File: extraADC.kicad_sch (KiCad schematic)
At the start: 21 parts, among them J10 G125-MH11005L1P, Q14 DMP2160UWQ-7, U42 ADS1015BQDGSRQ1, U43 ADS1015BQDGSRQ1

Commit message: Add some notes on progress
Signed-off-by: Corey Minyard <corey@minyard.net>
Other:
- note added: "I2C addr = 0x48"
- note added: "I2C addr = 0x49"
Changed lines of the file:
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@@
 	(generator_version "9.0")
 	(paper "A4")
+	(text "I2C addr = 0x48"
+		(exclude_from_sim no)
+		(at 183.388 76.708 0)
+		(effects
+			(font
+				(size 1.524 1.524)
+			)
+		)
+	)
+	(text "I2C addr = 0x49"
+		(exclude_from_sim no)
+		(at 174.498 115.57 0)
+		(effects
+			(font
+				(size 1.524 1.524)
+			)
+		)
+	)
 	(junction
 		(at 160.02 66.04)

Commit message: Add licensing
Use CERN-OHL-W version 2

Signed-off-by: Corey Minyard <corey@minyard.net>
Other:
- company: (none) -> AMSAT-NA
- title: (none) -> Extra ADC handled by the Antenna Control Processor
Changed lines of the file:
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@@
 	(generator_version "10.0")
 	(paper "A4")
+	(title_block
+		(title "Extra ADC handled by the Antenna Control Processor")
+		(date "2026-08-20")
+		(rev "4.0")
+		(company "AMSAT-NA")
+		(comment 1 "AE5KM")
+		(comment 2 "Copyright Corey Minyard, 2026")
+		(comment 3 "Licensed under CERN-OHL-W version 2")
+	)
 	(text "I2C addr = 0x48"
 		(exclude_from_sim no)

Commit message: Rework the antenna controller power
Change the MOSFET + ferrite to an inrush-controlled chip on the antenna
controller power and remove the separate ADC power enable.  Just power
the ADCs with the antenna controller power, there wasn't much benefit in
separate power control for it.

Signed-off-by: Corey Minyard <corey@minyard.net>
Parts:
- removed FB10: 1KΩ@100MHz, Inductor_SMD:L_0603_1608Metric_Pad1.05x0.95mm_HandSolder, symbol Device:FerriteBead_Small
- removed Q14: DMP2160UWQ-7, Package_TO_SOT_SMD:SOT-323_SC-70, symbol Transistor_FET:Q_PMOS_GSD
- removed R176: 10KΩ, Resistor_SMD:R_0402_1005Metric_Pad0.72x0.64mm_HandSolder, symbol Device:R
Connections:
- net ADC_3.3V renamed ANT_3.3V

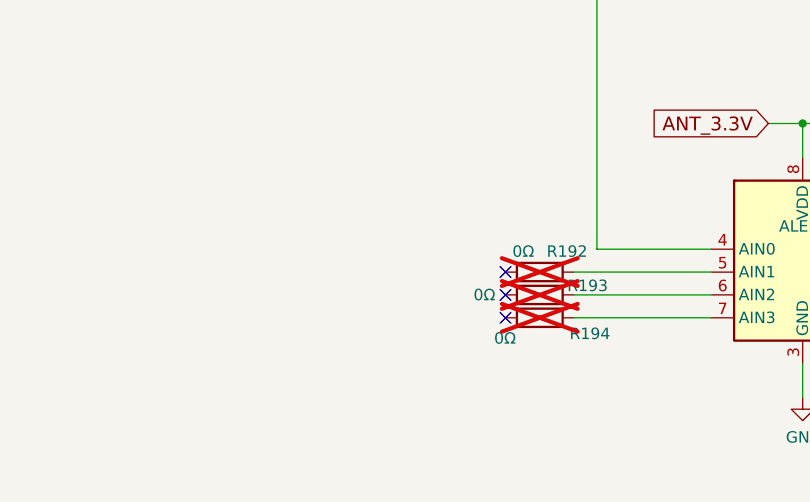
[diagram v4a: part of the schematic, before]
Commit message: Replaced the MOSFETs controlling USB power with an LM7310
It's a dual MOSFET ideal diode with an enable.  It should fix all the
USB power problems.

Signed-off-by: Corey Minyard <corey@minyard.net>
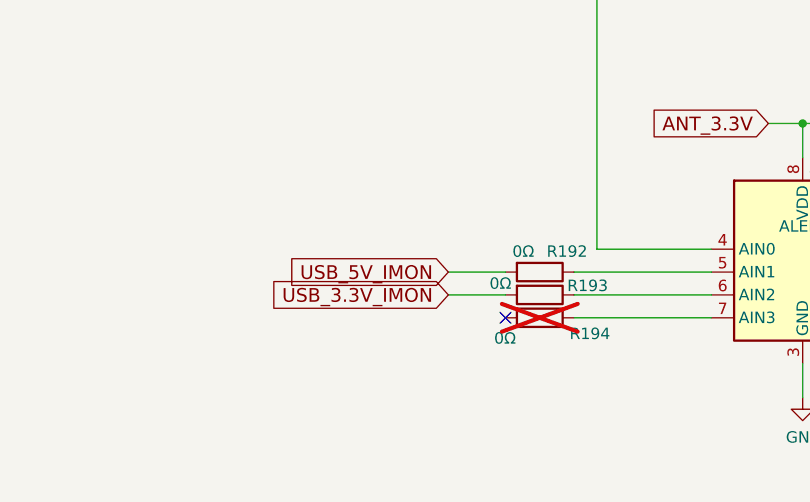
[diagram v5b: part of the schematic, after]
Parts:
- R192, R193: now fitted; now in the parts list
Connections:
- net USB_5V_IMON: now reaches R192.2
- net USB_3.3V_IMON: now reaches R193.2
- no-connect marks 5 -> 3
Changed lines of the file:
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@@
-	)
-	(no_connect
-		(at 127 137.16)
-	)
-	(no_connect
-		(at 127 134.62)
 	)
 	(no_connect
@@
 	(wire
 		(pts
+			(xy 120.65 134.62) (xy 127 134.62)
+		)
+		(stroke
+			(width 0)
+			(type default)
+		)
+	)
+	(wire
+		(pts
 			(xy 113.03 66.04) (xy 113.03 74.93)
 		)
@@
 	(wire
 		(pts
+			(xy 120.65 137.16) (xy 127 137.16)
+		)
+		(stroke
+			(width 0)
+			(type default)
+		)
+	)
+	(wire
+		(pts
 			(xy 149.86 58.42) (xy 160.02 58.42)
 		)
@@
 			(width 0)
 			(type default)
+		)
+	)
+	(global_label "USB_5V_IMON"
+		(shape input)
+		(at 120.65 134.62 180)
+		(fields_autoplaced yes)
+		(effects
+			(font
+				(size 1.524 1.524)
+			)
+			(justify right)
+		)
+		(property "Intersheetrefs" "${INTERSHEET_REFS}"
+			(at 102.5407 134.62 0)
+			(hide yes)
+			(show_name no)
+			(do_not_autoplace no)
+			(effects
+				(font
+					(size 1.27 1.27)
+				)
+				(justify right)
+			)
 		)
 	)
@@
 		(property "Intersheetrefs" "${INTERSHEET_REFS}"
 			(at 143.2533 118.11 0)
+			(hide yes)
+			(show_name no)
+			(do_not_autoplace no)
+			(effects
+				(font
+					(size 1.27 1.27)
+				)
+				(justify right)
+			)
+		)
+	)
+	(global_label "USB_3.3V_IMON"
+		(shape input)
+		(at 120.65 137.16 180)
+		(fields_autoplaced yes)
+		(effects
+			(font
+				(size 1.524 1.524)
+			)
+			(justify right)
+		)
+		(property "Intersheetrefs" "${INTERSHEET_REFS}"
+			(at 100.3636 137.16 0)
 			(hide yes)
 			(show_name no)
@@
 		(body_style 1)
 		(exclude_from_sim no)
-		(in_bom no)
+		(in_bom yes)
 		(on_board yes)
 		(in_pos_files yes)
-		(dnp yes)
+		(dnp no)
 		(property "Reference" "R192"
 			(at 131.572 132.334 90)
@@
 		(body_style 1)
 		(exclude_from_sim no)
-		(in_bom no)
+		(in_bom yes)
 		(on_board yes)
 		(in_pos_files yes)
-		(dnp yes)
+		(dnp no)
 		(property "Reference" "R193"
 			(at 133.858 136.144 90)
@@
 		)
 		(property "Value" "0Ω"
-			(at 123.444 137.16 90)
-			(show_name no)
-			(do_not_autoplace no)
+			(at 125.222 135.89 90)
+			(show_name no)
+			(do_not_autoplace no)

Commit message: Change all instances of K (for kilo) to k
That's the standard.

Signed-off-by: Corey Minyard <corey@minyard.net>
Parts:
- R168, R169, R170, R171, R172: value 4.7KΩ -> 4.7kΩ
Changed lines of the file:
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@@
 			)
 		)
-		(property "Value" "4.7KΩ"
+		(property "Value" "4.7kΩ"
 			(at 110.744 75.946 90)
 			(show_name no)
@@
 			)
 		)
-		(property "Value" "4.7KΩ"
+		(property "Value" "4.7kΩ"
 			(at 103.124 75.946 90)
 			(show_name no)
@@
 			)
 		)
-		(property "Value" "4.7KΩ"
+		(property "Value" "4.7kΩ"
 			(at 99.314 75.946 90)
 			(show_name no)
@@
 			)
 		)
-		(property "Value" "4.7KΩ"
+		(property "Value" "4.7kΩ"
 			(at 114.554 75.946 90)
 			(show_name no)
@@
 			)
 		)
-		(property "Value" "4.7KΩ"
+		(property "Value" "4.7kΩ"
 			(at 106.934 75.946 90)
 			(show_name no)
